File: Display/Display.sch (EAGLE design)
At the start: 30 parts, among them SW1 SWITCH-PTS-810, SW2 SWITCH-PTS-810, SW3 SWITCH-PTS-810, U1 ER-OLED0.95-2C, U2 FAN5331SX, U3 ATSAMD20E17A-AU, U4 MIC5205-3.3YM5 TR

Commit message: Various fixes
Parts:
- JP2: PARTNUM 147721-3 -> (none)
- R1: value 10KΩ -> 10K
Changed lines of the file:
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@@
 <part name="R3" library="Modulo" deviceset="RESISTOR" device="-10KΩ" value="10KΩ"/>
 <part name="R4" library="Modulo" deviceset="RESISTOR" device="-1KΩ" value="1KΩ"/>
-<part name="JP2" library="Modulo" deviceset="HEADER-1X4" device="-AMPMODU">
-<attribute name="PARTNUM" value="147721-3"/>
-</part>
-<part name="R1" library="Modulo" deviceset="RESISTOR" device="-10KΩ" value="10KΩ"/>
+<part name="JP2" library="Modulo" deviceset="HEADER-1X4" device="-AMPMODU"/>
+<part name="R1" library="Modulo" deviceset="RESISTOR" device="-10KΩ" value="10K"/>
 <part name="R5" library="Modulo" deviceset="RESISTOR" device="-10KΩ" value="10KΩ"/>
 <part name="R6" library="Modulo" deviceset="RESISTOR" device="-10KΩ" value="10KΩ"/>

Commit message: Various minor tweaks based on testing and feedback from manufacturer
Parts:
- PCB1: VERSION 3 -> 4
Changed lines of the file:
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@@
 <attribute name="BOARD" value="Display"/>
 <attribute name="PARTNUM" value="Display PCB"/>
-<attribute name="VERSION" value="3"/>
+<attribute name="VERSION" value="4"/>
 </part>
 <part name="SW1" library="Modulo" deviceset="SWITCH" device="-PTS-810" value="SWITCH-PTS-810"/>

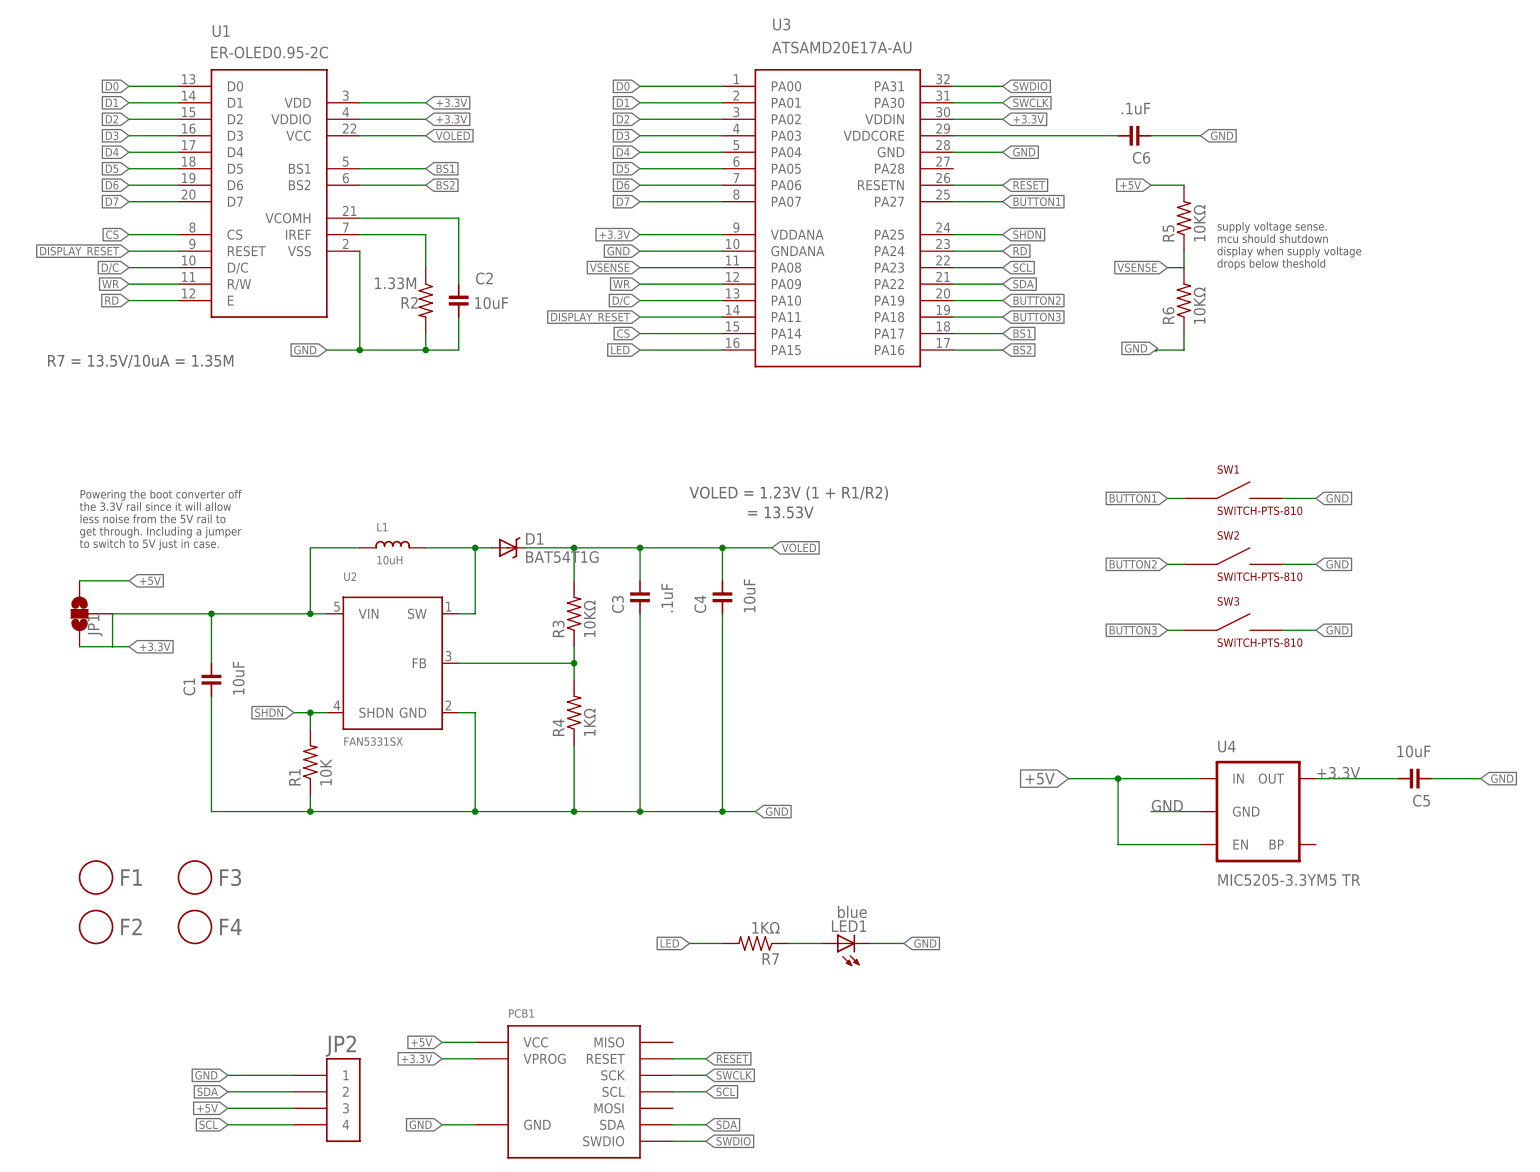
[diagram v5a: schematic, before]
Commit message: Added unique board prefixes to part numbers due to CM requirements
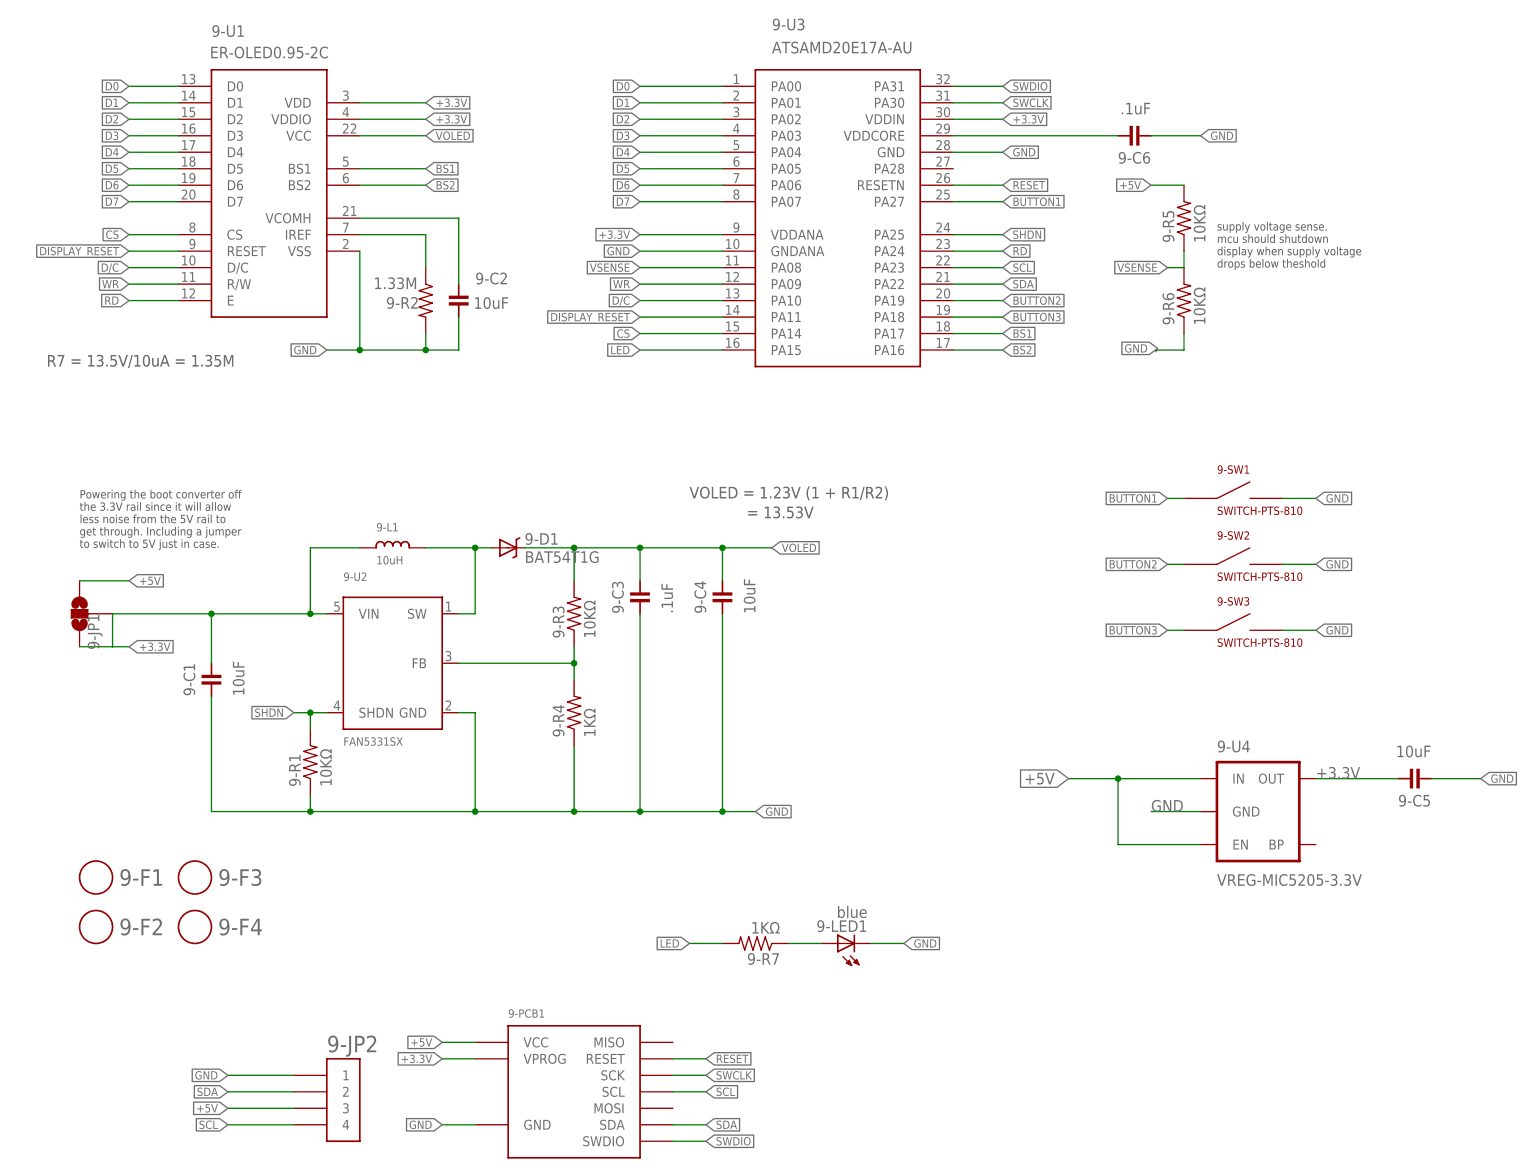
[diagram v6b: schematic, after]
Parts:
- 9-R1: value 10K -> 10KΩ
- 9-U4: value MIC5205-3.3YM5 TR -> VREG-MIC5205-3.3V
- renumbered C1 to 9-C1, C2 to 9-C2, C3 to 9-C3, C4 to 9-C4, C5 to 9-C5, C6 to 9-C6, D1 to 9-D1, F1 to 9-F1, F2 to 9-F2, F3 to 9-F3, F4 to 9-F4, JP1 to 9-JP1, JP2 to 9-JP2, L1 to 9-L1, LED1 to 9-LED1, PCB1 to 9-PCB1, R1 to 9-R1, R2 to 9-R2, R3 to 9-R3, R4 to 9-R4, R5 to 9-R5, R6 to 9-R6, R7 to 9-R7, SW1 to 9-SW1, SW2 to 9-SW2, SW3 to 9-SW3, U1 to 9-U1, U2 to 9-U2, U3 to 9-U3, U4 to 9-U4
